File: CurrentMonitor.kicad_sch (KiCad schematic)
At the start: 27 parts, among them J1 USB_B_Micro, J10 Screw_Terminal_01x02, J11 Barrel_Jack_Switch_SMT, J12 USB_A, J13 Conn_Coaxial, J2 Banana Red, J3 Banana Green, J4 Barrel_Jack_Switch_SMT, J5 Screw_Terminal_01x02, J6 Screw_Terminal_01x02, J7 Conn_02x03_Odd_Even, J8 Banana Red, J9 Banana Green

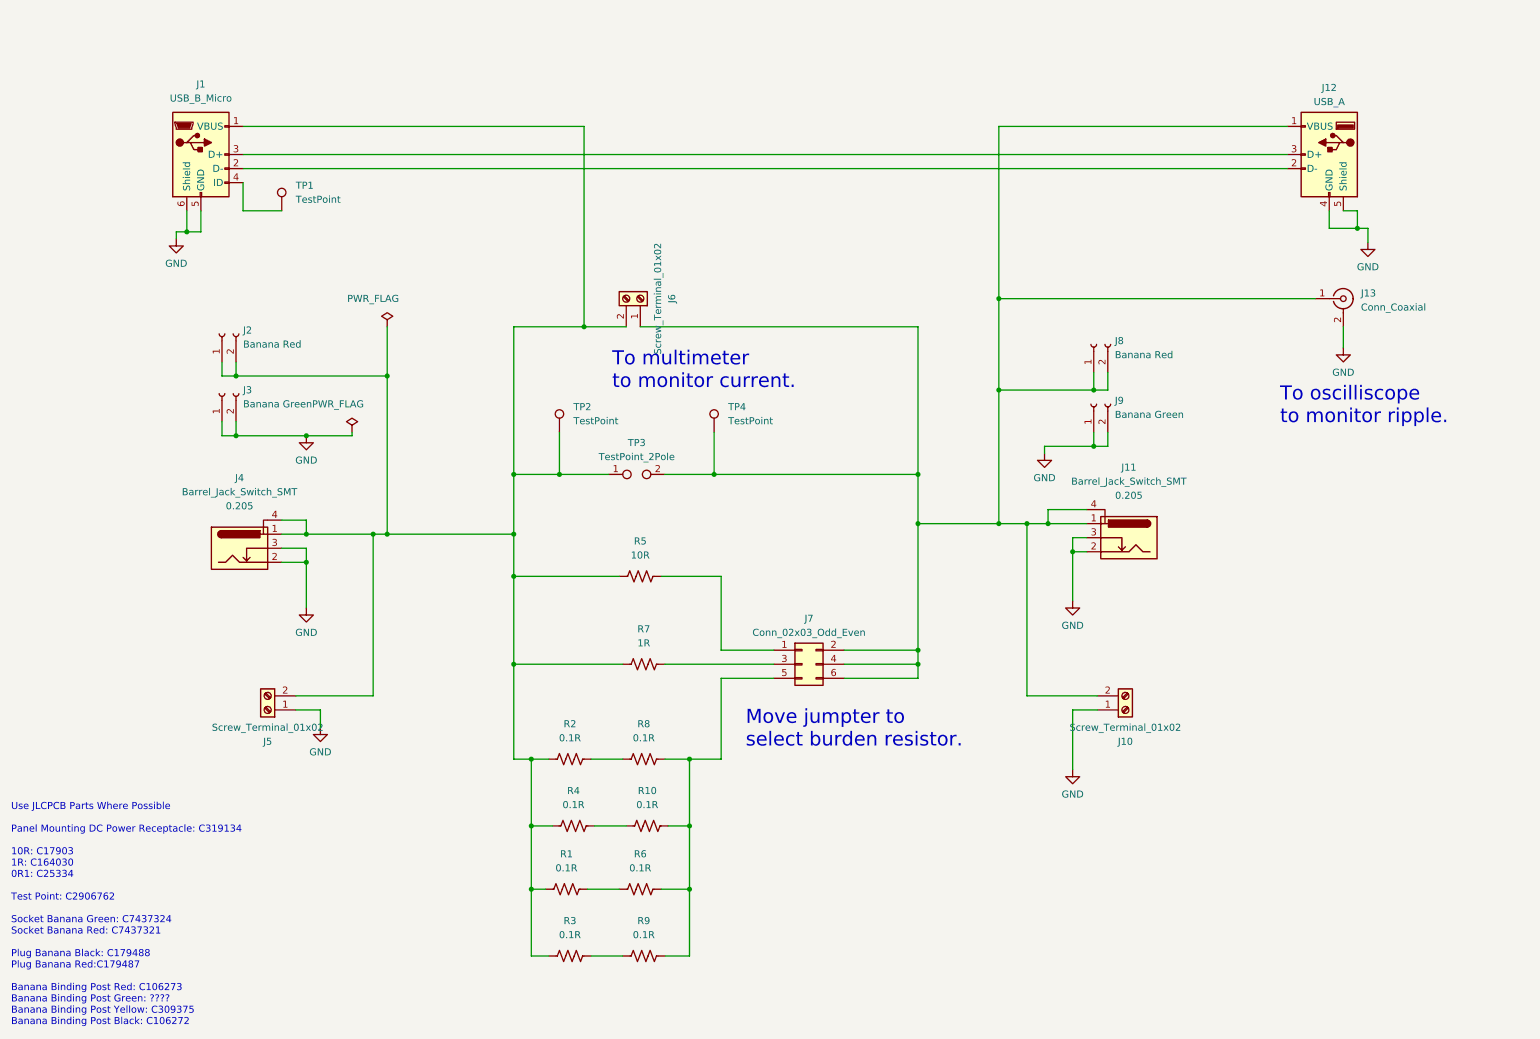
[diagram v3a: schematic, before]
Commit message: Initical placement of PCB components and edges. Still need USB parts.
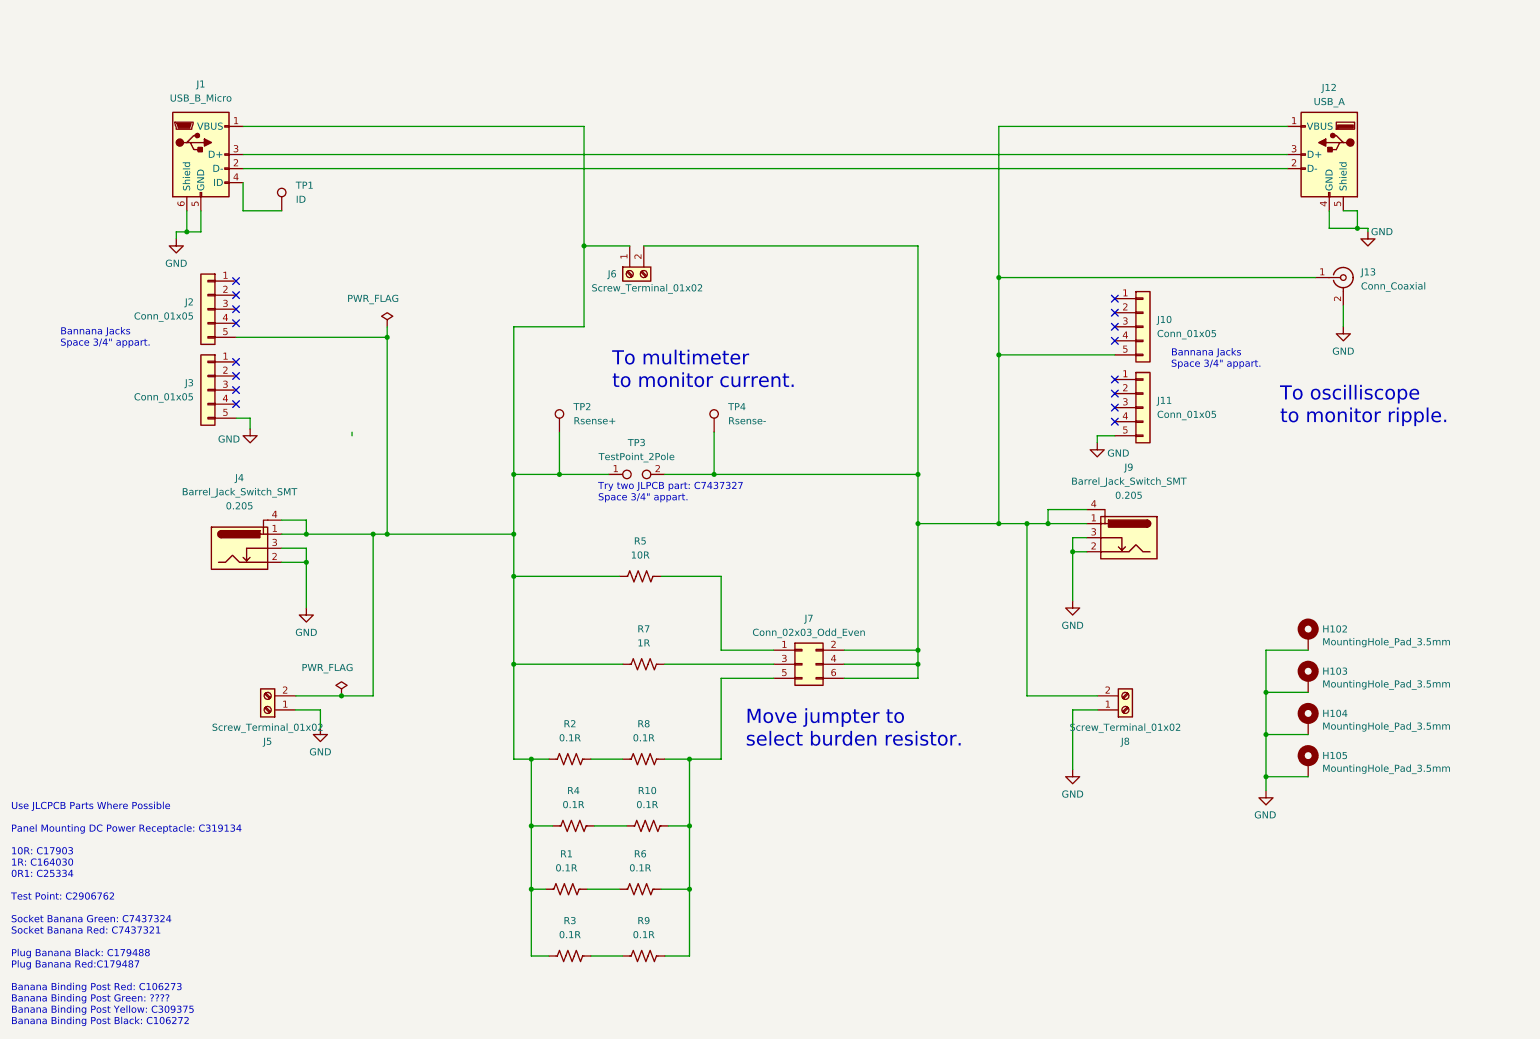
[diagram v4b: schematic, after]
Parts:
- removed J2, J8: Banana Red, symbol Connector:Conn_01x02_Socket
- removed J3, J9: Banana Green, symbol Connector:Conn_01x02_Socket
- added H102, H103, H104, H105: MountingHole_Pad_3.5mm, MountingHole:MountingHole_3.5mm_Pad_Via, symbol GPAD_SCH_LIB:MountingHole_Pad_3.5mm
- added J10, J11, J2, J3: Conn_01x05, Connector:Banana_Cliff_FCR7350x_S16N-PC_Horizontal, symbol Connector_Generic:Conn_01x05
- J1: Cost (none) -> 0.0329; Distributor 1 (none) -> JLCPCB; Distributor 1 PN (none) -> C404969
- J12: Cost (none) -> 0.0290; Distributor 1 (none) -> JLCPCB; Distributor 1 PN (none) -> C3038692
- J13: footprint (none) -> BNC_Amphenol_B6252HB-NPP3G-50_Horizontal; Cost (none) -> 4.1175; Distributor 1 (none) -> JLCPCB; Distributor 1 PN (none) -> C305920
- J5, J6: footprint (none) -> TerminalBlock_Phoenix_MKDS-1,5-2_1x02_P5.00mm_Horizontal; Cost (none) -> 0.0764
- J7: footprint (none) -> Connector_PinHeader_2.54mm:PinHeader_2x03_P2.54mm_Vertical; Cost (none) -> 0.0486
- J8: renamed from J10; footprint (none) -> TerminalBlock_Phoenix_MKDS-1,5-2_1x02_P5.00mm_Horizontal; Cost (none) -> 0.0764
- R1, R10, R2, R3, R4, R6, R8, R9: footprint (none) -> Resistor_SMD:R_1206_3216Metric_Pad1.30x1.75mm_HandSolder; Cost (none) -> 0.0047
- R5: footprint (none) -> Resistor_SMD:R_1206_3216Metric_Pad1.30x1.75mm_HandSolder; Cost (none) -> 0.0028
- R7: footprint (none) -> Resistor_SMD:R_1206_3216Metric_Pad1.30x1.75mm_HandSolder; Cost (none) -> 0.0042
- TP1: value TestPoint -> ID; footprint (none) -> TestPoint:TestPoint_Loop_D2.50mm_Drill1.0mm; Cost (none) -> 0.0696; Distributor 1 PN C2906762 -> C5277086
- TP2: value TestPoint -> Rsense+; footprint (none) -> TestPoint:TestPoint_Loop_D2.50mm_Drill1.0mm; Cost (none) -> 0.0696; Distributor 1 PN C2906762 -> C5277086
- TP3: footprint (none) -> Connector:Banana_Jack_2Pin
- TP4: value TestPoint -> Rsense-; footprint (none) -> TestPoint:TestPoint_Loop_D2.50mm_Drill1.0mm; Cost (none) -> 0.0696; Distributor 1 PN C2906762 -> C5277086
- renumbered J11 to J9
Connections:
- net GND: now also H102.1, H103.1, H104.1, H105.1, J11.5 (Pin_5), J3.5 (Pin_5)
- net at J1.1 (VBUS), J4.1, J4.4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: now also J6.1 (Pin_1), J2.5 (Pin_5); no longer J6.2 (Pin_2)
- net at J12.1 (VBUS), J13.1 (In), J7.2 (Pin_2)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: now also J6.2 (Pin_2), J10.5 (Pin_5); no longer J6.1 (Pin_1)
- no-connect marks 0 -> 16
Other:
- note added: "Bannana Jacks Space 3/4" appart."
- note added: "Try two JLPCB part: C7437327 Space 3/4" appart."
- moved on the sheet: J13, J6

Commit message: Add another bananna jack option. Get 3D foot prints working for Barrel Jack.
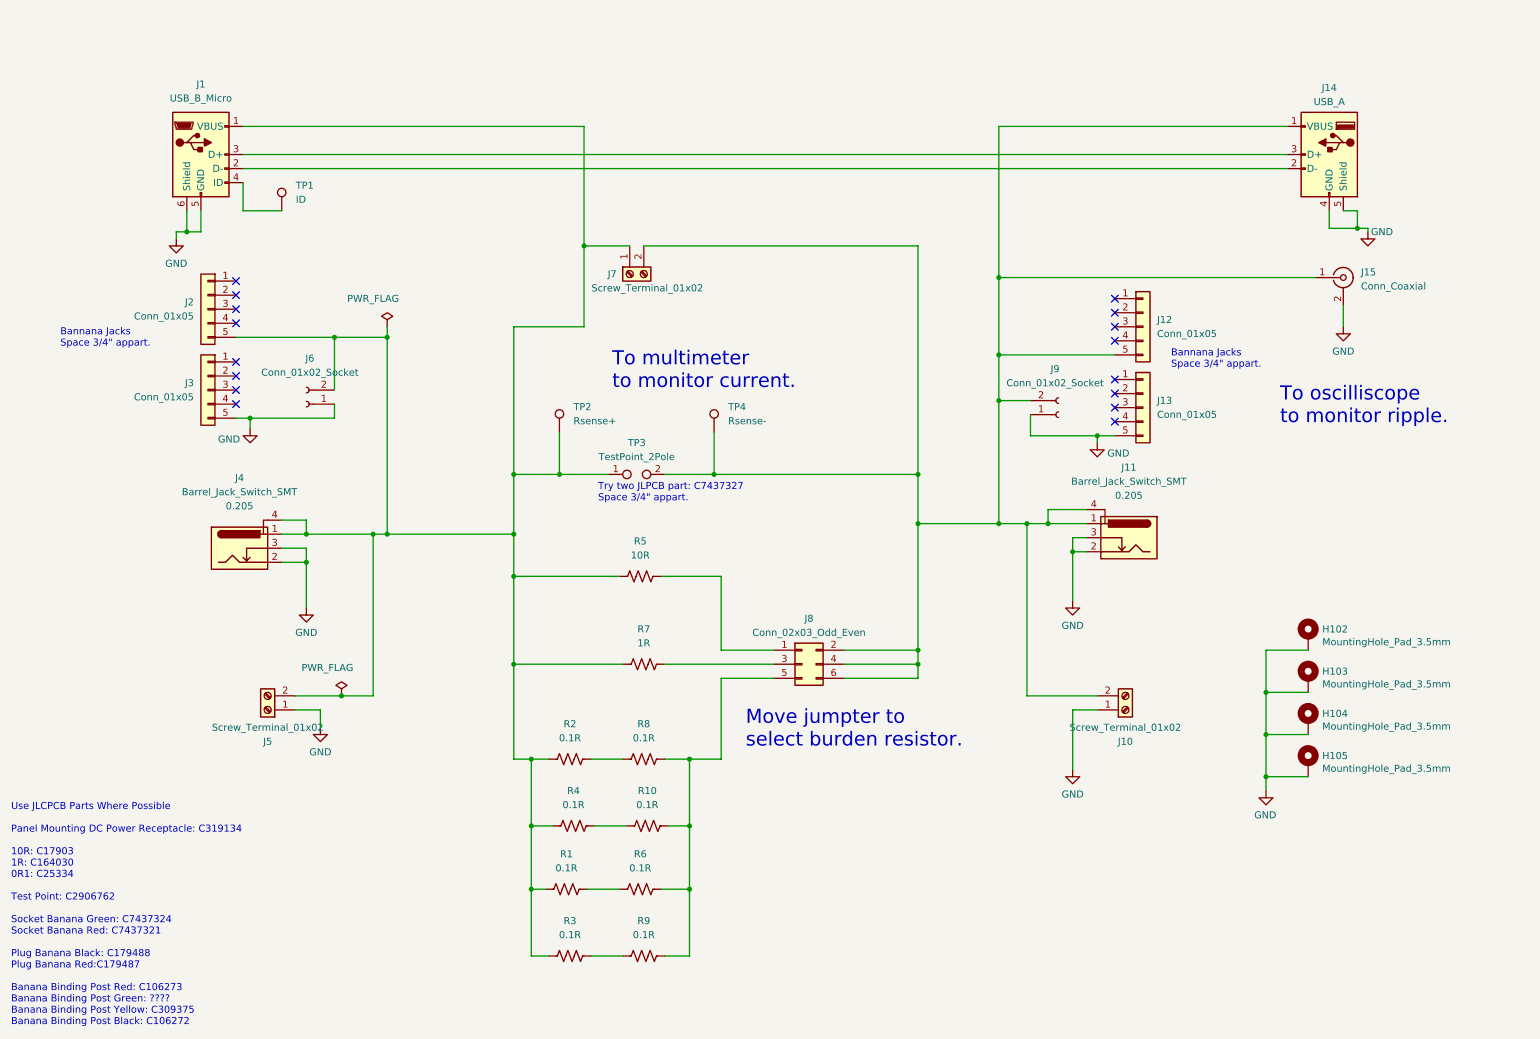
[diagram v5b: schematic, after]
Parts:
- added J6, J9: Conn_01x02_Socket, Connector:Banana_Jack_2Pin, symbol Connector:Conn_01x02_Socket
- J11: renamed from J9; footprint GeneralPurposeAlarmDevicePCB:BarrelJack_CLIFF_FC681465S_SMT_Horizontal -> Connector_BarrelJack:BarrelJack_CLIFF_FC681465S_SMT_Horizontal
- J4: footprint GeneralPurposeAlarmDevicePCB:BarrelJack_CLIFF_FC681465S_SMT_Horizontal -> Connector_BarrelJack:BarrelJack_CLIFF_FC681465S_SMT_Horizontal
- renumbered J8 to J10, J10 to J12, J11 to J13, J12 to J14, J13 to J15, J6 to J7, J7 to J8
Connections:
- net GND: now also J6.1 (Pin_1), J9.1 (Pin_1)
- net at J1.1 (VBUS), J2.5 (Pin_5), J4.1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: now also J6.2 (Pin_2)
- net at J10.2 (Pin_2), J11.1, J11.4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: now also J9.2 (Pin_2)
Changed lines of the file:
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@@
   (junction (at 121.285 54.61) (diameter 0) (color 0 0 0 0)
   )
+  (junction (at 60.96 85.725) (diameter 0) (color 0 0 0 0)
+  )
   (junction (at 77.47 135.89) (diameter 0) (color 0 0 0 0)
   )
@@
   (junction (at 111.76 147.32) (diameter 0) (color 0 0 0 0)
   )
+  (junction (at 76.2 71.12) (diameter 0) (color 0 0 0 0)
+  )
+  (junction (at 196.215 82.55) (diameter 0) (color 0 0 0 0)
+  )
   (junction (at 116.84 95.885) (diameter 0) (color 0 0 0 0)
+  )
+  (junction (at 213.995 88.9) (diameter 0) (color 0 0 0 0)
   )
   (no_connect (at 217.17 86.36))
@@
   (no_connect (at 58.42 78.105))
   (no_connect (at 58.42 80.645))
+  (wire (pts (xy 76.2 83.185) (xy 76.2 85.725))
+    (stroke (width 0) (type default))
+  )
   (wire (pts (xy 205.105 102.235) (xy 212.09 102.235))
     (stroke (width 0) (type default))
@@
     (stroke (width 0) (type default))
   )
-  (wire (pts (xy 79.375 88.265) (xy 79.375 88.9))
-    (stroke (width 0) (type default))
-  )
   (wire (pts (xy 209.55 109.855) (xy 212.09 109.855))
     (stroke (width 0) (type default))
   )
-  (wire (pts (xy 196.215 74.295) (xy 196.215 104.775))
+  (wire (pts (xy 196.215 74.295) (xy 196.215 82.55))
     (stroke (width 0) (type default))
   )
@@
     (stroke (width 0) (type default))
   )
-  (wire (pts (xy 58.42 71.12) (xy 85.725 71.12))
+  (wire (pts (xy 58.42 71.12) (xy 76.2 71.12))
     (stroke (width 0) (type default))
   )
@@
     (stroke (width 0) (type default))
   )
+  (wire (pts (xy 213.995 88.9) (xy 217.17 88.9))
+    (stroke (width 0) (type default))
+  )
   (wire (pts (xy 209.55 109.855) (xy 209.55 118.745))
     (stroke (width 0) (type default))
@@
     (stroke (width 0) (type default))
   )
+  (wire (pts (xy 76.2 71.12) (xy 76.2 80.645))
+    (stroke (width 0) (type default))
+  )
   (wire (pts (xy 260.985 48.26) (xy 260.985 51.435))
     (stroke (width 0) (type default))
   )
+  (wire (pts (xy 60.96 85.725) (xy 76.2 85.725))
+    (stroke (width 0) (type default))
+  )
   (wire (pts (xy 201.295 104.775) (xy 201.295 135.89))
     (stroke (width 0) (type default))
@@
     (stroke (width 0) (type default))
   )
+  (wire (pts (xy 76.2 71.12) (xy 85.725 71.12))
+    (stroke (width 0) (type default))
+  )
   (wire (pts (xy 244.475 150.495) (xy 244.475 153.035))
     (stroke (width 0) (type default))
@@
     (stroke (width 0) (type default))
   )
+  (wire (pts (xy 201.93 85.09) (xy 201.93 88.9))
+    (stroke (width 0) (type default))
+  )
   (wire (pts (xy 85.725 106.68) (xy 108.585 106.68))
     (stroke (width 0) (type default))
@@
     (stroke (width 0) (type default))
   )
+  (wire (pts (xy 196.215 82.55) (xy 196.215 104.775))
+    (stroke (width 0) (type default))
+  )
   (wire (pts (xy 260.985 51.435) (xy 262.89 51.435))
     (stroke (width 0) (type default))
@@
     (stroke (width 0) (type default))
   )
+  (wire (pts (xy 196.215 82.55) (xy 201.93 82.55))
+    (stroke (width 0) (type default))
+  )
   (wire (pts (xy 168.275 132.715) (xy 181.61 132.715))
     (stroke (width 0) (type default))
@@
     (stroke (width 0) (type default))
   )
-  (wire (pts (xy 217.17 88.9) (xy 213.995 88.9))
+  (wire (pts (xy 201.93 88.9) (xy 213.995 88.9))
     (stroke (width 0) (type default))
   )
@@
       (effects (font (size 1.27 1.27)))
     )
-    (property "Footprint" "GeneralPurposeAlarmDevicePCB:BarrelJack_CLIFF_FC681465S_SMT_Horizontal" (at 60.325 110.236 0)
+    (property "Footprint" "Connector_BarrelJack:BarrelJack_CLIFF_FC681465S_SMT_Horizontal" (at 60.325 110.236 0)
       (effects (font (size 1.27 1.27)) hide)
     )
@@
   (symbol (lib_id "Connector:USB_A") (at 255.905 38.1 0) (mirror y) (unit 1)
     (in_bom yes) (on_board yes) (dnp no)
-    (property "Reference" "J12" (at 255.905 26.035 0)
+    (property "Reference" "J14" (at 255.905 26.035 0)
       (effects (font (size 1.27 1.27)))
     )
@@
       (project "CurrentMonitor"
         (path "/c2625580-5dc2-4487-938a-c703153fa89f"
-          (reference "J12") (unit 1)
+          (reference "J14") (unit 1)
         )
       )
@@
     )
   )
+  (symbol (lib_id "Connector:Conn_01x02_Socket") (at 71.12 83.185 180) (unit 1)
+    (in_bom no) (on_board yes) (dnp no) (fields_autoplaced)
+    (property "Reference" "J6" (at 71.755 74.93 0)
+      (effects (font (size 1.27 1.27)))
+    )
+    (property "Value" "Conn_01x02_Socket" (at 71.755 77.47 0)
+      (effects (font (size 1.27 1.27)))
+    )
+    (property "Footprint" "Connector:Banana_Jack_2Pin" (at 71.12 83.185 0)
+      (effects (font (size 1.27 1.27)) hide)
+    )
+    (property "Datasheet" "~" (at 71.12 83.185 0)
+      (effects (font (size 1.27 1.27)) hide)
+    )
+    (pin "1")
+    (pin "2")
+    (instances
+      (project "CurrentMonitor"
+        (path "/c2625580-5dc2-4487-938a-c703153fa89f"
+          (reference "J6") (unit 1)
+        )
+      )
+    )
+  )
   (symbol (lib_id "Connector_Generic:Conn_02x03_Odd_Even") (at 160.655 130.175 0) (unit 1)
     (in_bom yes) (on_board yes) (dnp no) (fields_autoplaced)
-    (property "Reference" "J7" (at 161.925 121.92 0)
+    (property "Reference" "J8" (at 161.925 121.92 0)
       (effects (font (size 1.27 1.27)))
     )
@@
       (project "CurrentMonitor"
         (path "/c2625580-5dc2-4487-938a-c703153fa89f"
-          (reference "J7") (unit 1)
+          (reference "J8") (unit 1)
         )
       )
@@
   (symbol (lib_id "Connector:Screw_Terminal_01x02") (at 219.075 138.43 0) (mirror x) (unit 1)
     (in_bom yes) (on_board yes) (dnp no)
-    (property "Reference" "J8" (at 219.075 144.145 0)
+    (property "Reference" "J10" (at 219.075 144.145 0)
       (effects (font (size 1.27 1.27)))
     )
@@
       (project "CurrentMonitor"
         (path "/c2625580-5dc2-4487-938a-c703153fa89f"
-          (reference "J8") (unit 1)
+          (reference "J10") (unit 1)
         )
       )
@@
   (symbol (lib_id "Connector_Generic:Conn_01x05") (at 222.25 69.215 0) (unit 1)
     (in_bom yes) (on_board yes) (dnp no) (fields_autoplaced)
-    (property "Reference" "J10" (at 224.79 67.945 0)
+    (property "Reference" "J12" (at 224.79 67.945 0)
       (effects (font (size 1.27 1.27)) (justify left))
     )
@@
       (project "CurrentMonitor"
         (path "/c2625580-5dc2-4487-938a-c703153fa89f"
-          (reference "J10") (unit 1)
+          (reference "J12") (unit 1)
         )
       )
@@
   (symbol (lib_id "PubInv_KiCad_SCH_LIB:Barrel_Jack_Switch_SMT") (at 219.71 107.315 0) (mirror y) (unit 1)
     (in_bom yes) (on_board yes) (dnp no)
-    (property "Reference" "J9" (at 219.71 94.615 0)
+    (property "Reference" "J11" (at 219.71 94.615 0)
       (effects (font (size 1.27 1.27)))
     )
@@
       (effects (font (size 1.27 1.27)))
     )
-    (property "Footprint" "GeneralPurposeAlarmDevicePCB:BarrelJack_CLIFF_FC681465S_SMT_Horizontal" (at 218.44 108.331 0)
+    (property "Footprint" "Connector_BarrelJack:BarrelJack_CLIFF_FC681465S_SMT_Horizontal" (at 218.44 108.331 0)
       (effects (font (size 1.27 1.27)) hide)
     )
@@
       (project "CurrentMonitor"
         (path "/c2625580-5dc2-4487-938a-c703153fa89f"
-          (reference "J9") (unit 1)
+          (reference "J11") (unit 1)
         )
       )
@@
     )
   )
+  (symbol (lib_id "Connector:Conn_01x02_Socket") (at 207.01 85.09 0) (mirror x) (unit 1)
+    (in_bom no) (on_board yes) (dnp no)
+    (property "Reference" "J9" (at 206.375 76.835 0)
+      (effects (font (size 1.27 1.27)))
+    )
+    (property "Value" "Conn_01x02_Socket" (at 206.375 79.375 0)
+      (effects (font (size 1.27 1.27)))
+    )
+    (property "Footprint" "Connector:Banana_Jack_2Pin" (at 207.01 85.09 0)
+      (effects (font (size 1.27 1.27)) hide)
+    )
+    (property "Datasheet" "~" (at 207.01 85.09 0)
+      (effects (font (size 1.27 1.27)) hide)
+    )
+    (pin "1")
+    (pin "2")
+    (instances
+      (project "CurrentMonitor"
+        (path "/c2625580-5dc2-4487-938a-c703153fa89f"
+          (reference "J9") (unit 1)
+        )
+      )
+    )
+  )
   (symbol (lib_id "Connector:Screw_Terminal_01x02") (at 129.54 59.69 90) (mirror x) (unit 1)
     (in_bom yes) (on_board yes) (dnp no)
-    (property "Reference" "J6" (at 126.365 59.69 90)
+    (property "Reference" "J7" (at 126.365 59.69 90)
       (effects (font (size 1.27 1.27)))
     )
@@
       (project "CurrentMonitor"
         (path "/c2625580-5dc2-4487-938a-c703153fa89f"
-          (reference "J6") (unit 1)
+          (reference "J7") (unit 1)
         )
       )
@@
   (symbol (lib_id "Connector:Conn_Coaxial") (at 258.445 60.325 0) (unit 1)
     (in_bom yes) (on_board yes) (dnp no) (fields_autoplaced)
-    (property "Reference" "J13" (at 261.62 59.3482 0)
+    (property "Reference" "J15" (at 261.62 59.3482 0)
       (effects (font (size 1.27 1.27)) (justify left))
     )
@@
       (project "CurrentMonitor"
         (path "/c2625580-5dc2-4487-938a-c703153fa89f"
-          (reference "J13") (unit 1)
+          (reference "J15") (unit 1)
         )
       )
@@
   (symbol (lib_id "Connector_Generic:Conn_01x05") (at 222.25 83.82 0) (unit 1)
     (in_bom yes) (on_board yes) (dnp no) (fields_autoplaced)
-    (property "Reference" "J11" (at 224.79 82.55 0)
+    (property "Reference" "J13" (at 224.79 82.55 0)
       (effects (font (size 1.27 1.27)) (justify left))
     )
@@
       (project "CurrentMonitor"
         (path "/c2625580-5dc2-4487-938a-c703153fa89f"
-          (reference "J11") (unit 1)
-        )
-      )
+          (reference "J13") (unit 1)
+        )
+      )
